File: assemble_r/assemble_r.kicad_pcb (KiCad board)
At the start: 2 copper layers, 135 x 119.3 mm, 61 parts, among them J1 Conn_01x02_Pin, SW29 SW_Push, SW30 SW_Push, SW31 SW_Push, SW32 SW_Push, SW33 SW_Push, SW34 SW_Push, SW35 SW_Push, SW36 SW_Push, SW37 SW_Push, SW38 SW_Push, SW39 SW_Push, SW40 SW_Push, SW41 SW_Push, SW42 SW_Push, SW43 SW_Push, SW44 SW_Push, SW45 SW_Push, SW46 SW_Push, SW47 SW_Push, SW48 SW_Push, SW49 SW_Push, SW50 SW_Push, SW51 SW_Push, SW52 SW_Push, SW53 SW_Push, SW54 SW_Push, SW55 SW_Push, SW56 SW_Push, U1 Micon_BLEMicroPro

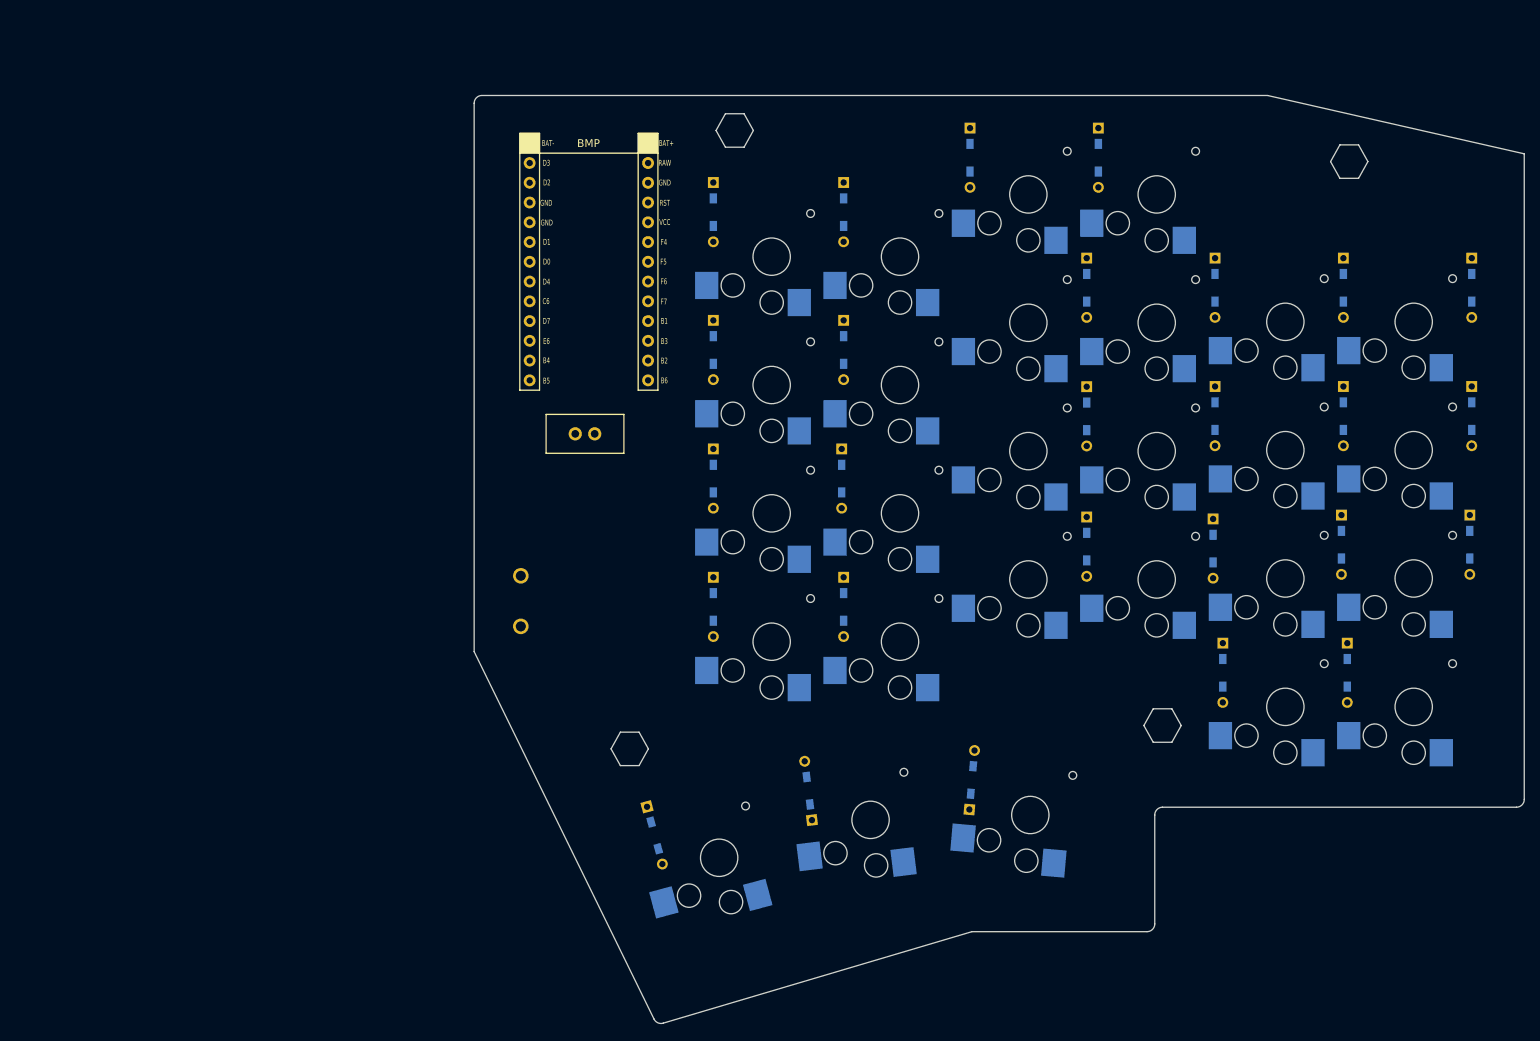
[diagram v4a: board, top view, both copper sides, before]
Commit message: feat: change key placement
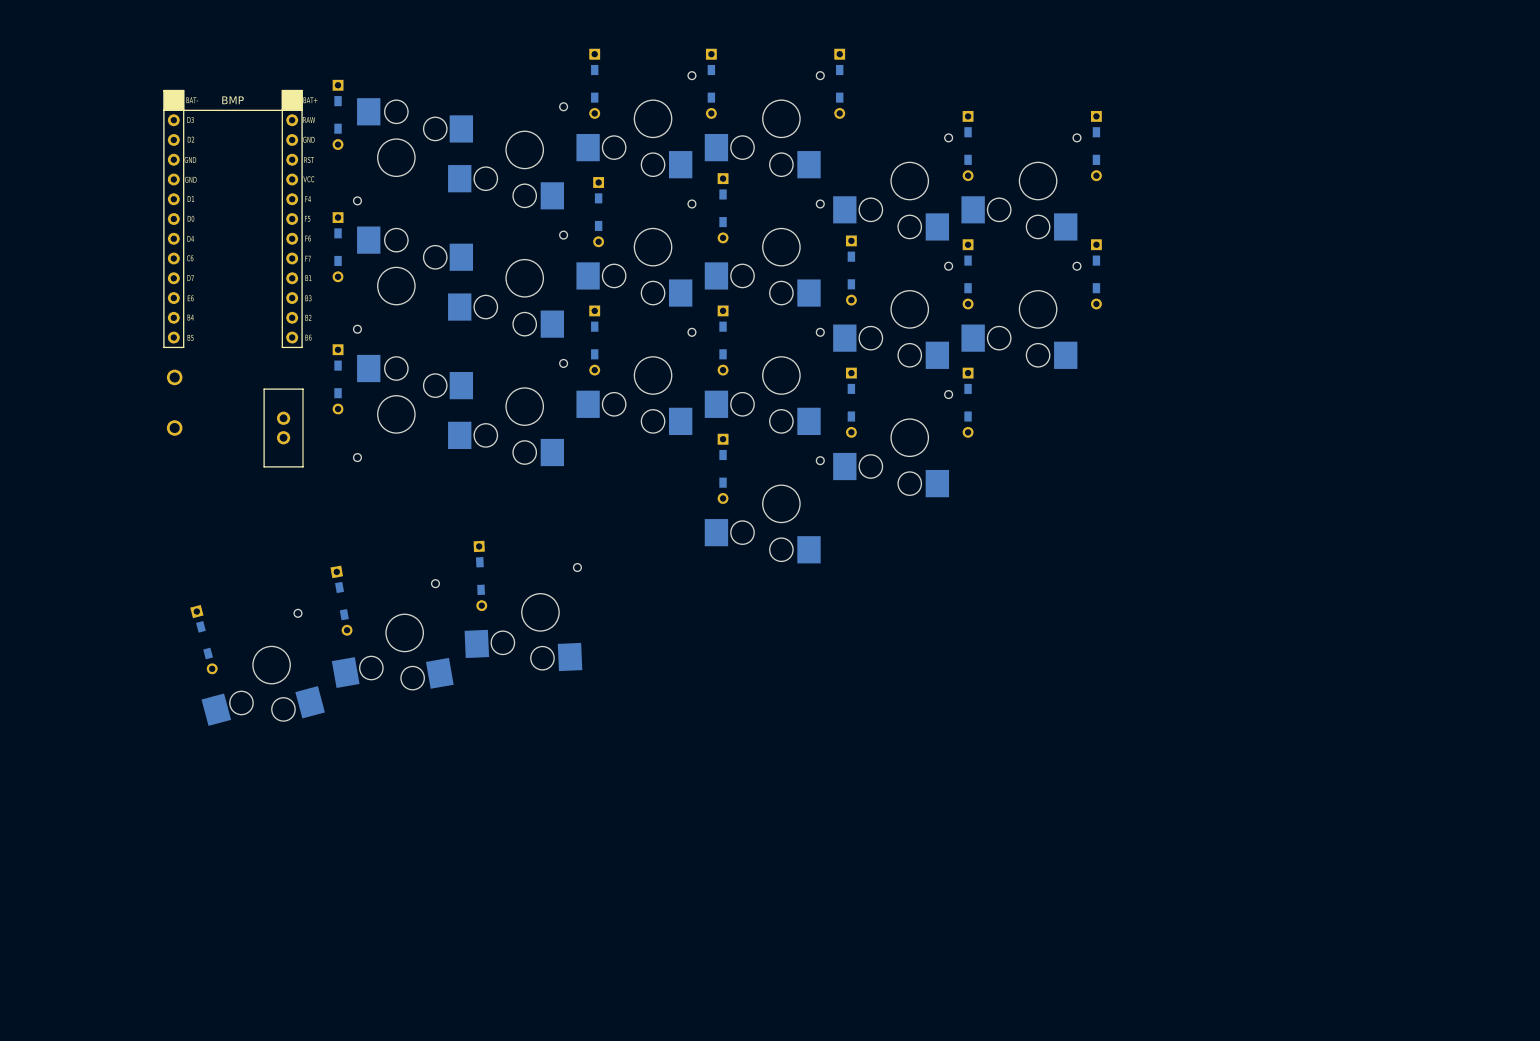
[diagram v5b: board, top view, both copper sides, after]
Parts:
- removed D44, D45, D46, D47, D48, D49, D50, D51, D52, D53, D54, D55: D, kbd_Parts:Diode_TH_SMD
- removed J1: Conn_01x02_Pin, kbd_Parts:Battery_2pin
- removed Ref** (x4): Val**, kbd_Hole:m2_Spacer_Hole_hex
- removed SW45, SW46, SW47, SW48, SW49, SW50, SW51, SW52, SW53, SW54, SW55: SW_Push, kbd_SW:Choc_v2_Hotswap_1u_16.5
- removed SW56: SW_Push, kbd_Parts:ResetSW
- removed U1: Micon_BLEMicroPro, kbd_Parts:Micon_BMP_7sKB
- added D23: D, kbd_Parts:Diode_TH_SMD, F.Cu at (63.5, 42.5)
- added D24: D, kbd_Parts:Diode_TH_SMD, F.Cu at (63.5, 59.5)
- added D25: D, kbd_Parts:Diode_TH_SMD, F.Cu at (63.5, 76.5)
- added D26: D, kbd_Parts:Diode_TH_SMD, F.Cu at (46.3, 110.0)
- added D27: D, kbd_Parts:Diode_TH_SMD, F.Cu at (96.5, 38.5)
- added D28: D, kbd_Parts:Diode_TH_SMD, F.Cu at (97.0, 55.0)
- added J23: Conn_01x02_Pin, kbd_Parts:Battery_2pin, F.Cu at (56.5, 82.8)
- added SW23: SW_Push, kbd_SW:Choc_v2_Hotswap_1u_16.5, F.Cu at (71.0, 48.0)
- added SW24: SW_Push, kbd_SW:Choc_v2_Hotswap_1u_16.5, F.Cu at (71.0, 64.5)
- added SW25: SW_Push, kbd_SW:Choc_v2_Hotswap_1u_16.5, F.Cu at (71.0, 81.0)
- added SW26: SW_Push, kbd_SW:Choc_v2_Hotswap_1u_16.5, F.Cu at (55.0, 113.2)
- added SW27: SW_Push, kbd_SW:Choc_v2_Hotswap_1u_16.5, F.Cu at (87.5, 47.0)
- added SW28: SW_Push, kbd_SW:Choc_v2_Hotswap_1u_16.5, F.Cu at (87.5, 63.5)
- added U23: Micon_BLEMicroPro, kbd_Parts:Micon_BMP_7sKB, F.Cu at (50.0, 57.7)
- SW44: footprint kbd_SW:Choc_v2_Hotswap_1u_16.5 -> kbd_Parts:ResetSW
- moved SW44 129.1 mm to (42.5, 79.5), turned to 90 degrees
- moved D43 66.9 mm to (161.0, 63.0), turned to -90 degrees
- moved D34 66.1 mm to (81.8, 101.8), turned to -87.5 degrees
- moved SW34 65.0 mm to (89.5, 106.4), turned to 2.5 degrees
- moved SW43 65.0 mm to (153.5, 67.5), turned to 0 degrees
- moved D33 64.2 mm to (113.0, 71.5), turned to -90 degrees
- moved SW33 62.6 mm to (104.0, 76.0), turned to 0 degrees
- moved D30 57.6 mm to (64.0, 105.0), turned to -80 degrees
- moved SW30 56.9 mm to (72.1, 109.1), turned to 10 degrees
- moved SW31 53.0 mm to (104.0, 43.0)
- moved SW32 53.0 mm to (104.0, 59.5)
- moved D42 51.5 mm to (161.0, 46.5)
- moved D32 51.3 mm to (113.0, 54.5)
- moved SW42 51.2 mm to (153.5, 51.0)
- moved D31 50.8 mm to (111.5, 38.5)
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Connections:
- D29 pad 1: Row0 -> Row2
- D30 pad 1: Row1 -> Row3
- D31 pad 1: Row2 -> Row0
- D32 pad 1: Row3 -> Row1
- D33 pad 1: Row4 -> Row2
- D34 pad 1: Row0 -> Row3
- D35 pad 1: Row1 -> Row0
- D36 pad 1: Row2 -> Row1
- D37 pad 1: Row3 -> Row2
- D38 pad 1: Row4 -> Row3
- D42 pad 1: Row3 -> Row0
- D43 pad 1: Row4 -> Row1
- SW29 pad 1: Col0 -> Col1
- SW30 pad 1: Col0 -> Col1
- SW31 pad 1: Col0 -> Col2
- SW32 pad 1: Col0 -> Col2
- SW33 pad 1: Col0 -> Col2
- SW34 pad 1: Col1 -> Col2
- SW35 pad 1: Col1 -> Col3
- SW36 pad 1: Col1 -> Col3
- SW37 pad 1: Col1 -> Col3
- SW38 pad 1: Col1 -> Col3
- SW39 pad 1: Col2 -> Col4
- SW40 pad 1: Col2 -> Col4
- SW41 pad 1: Col2 -> Col4
- SW42 pad 1: Col2 -> Col5
- SW43 pad 1: Col2 -> Col5
- SW44 pad 1: Col3 -> Reset
- SW44 pad 2: Net-(D44-A) -> GND
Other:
- board outline removed

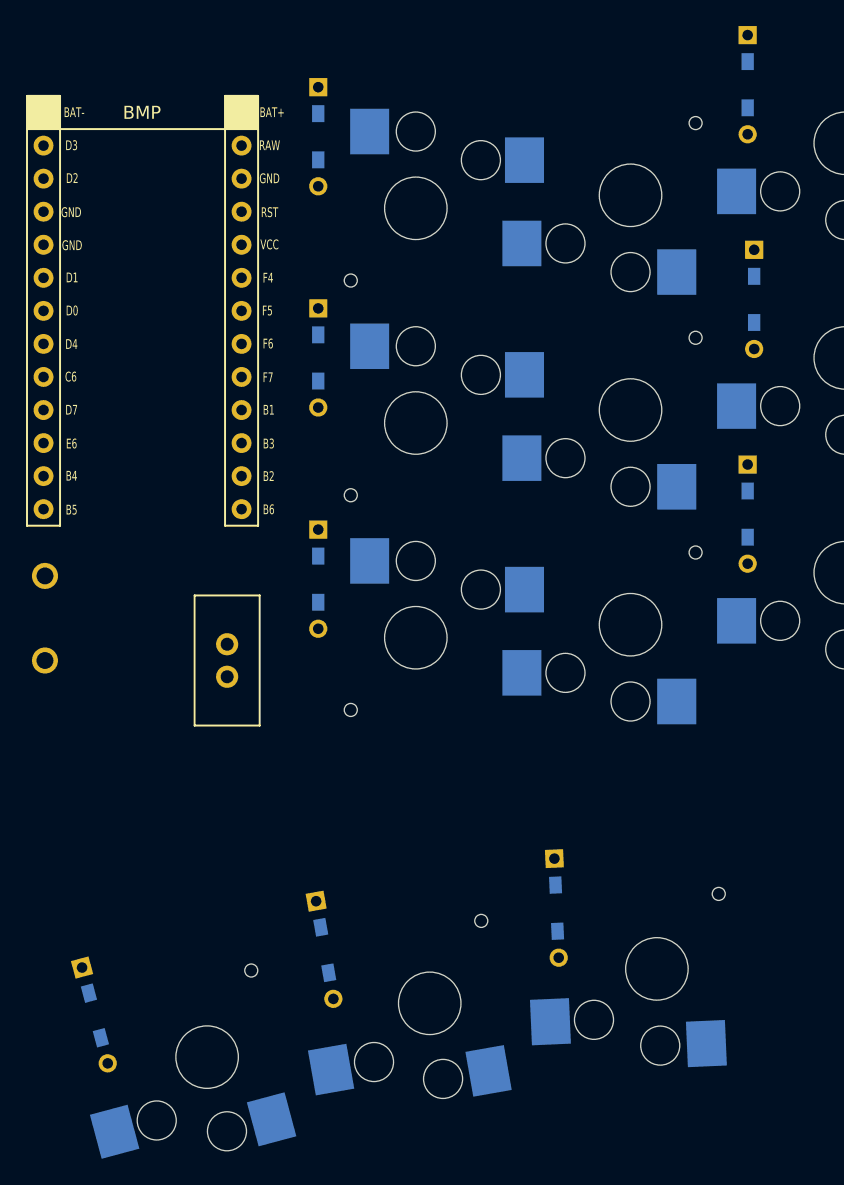
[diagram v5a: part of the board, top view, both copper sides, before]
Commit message: fix: key layout
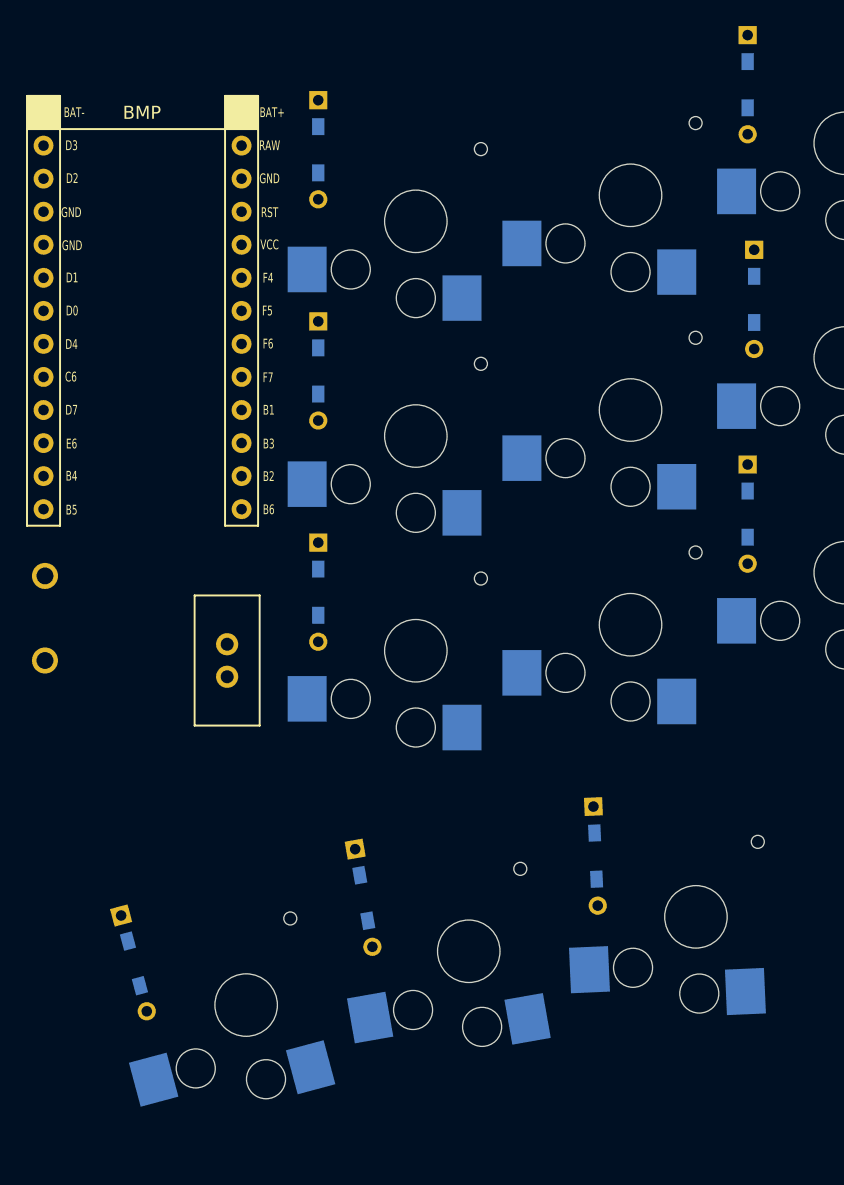
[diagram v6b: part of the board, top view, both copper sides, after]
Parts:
- moved D26 5.00 mm to (49.3, 106.0)
- moved D30 5.00 mm to (67.0, 101.0)
- moved D34 5.00 mm to (84.8, 97.8)
- moved SW26 5.00 mm to (58.0, 109.2)
- moved SW30 5.00 mm to (75.1, 105.1)
- moved SW34 5.00 mm to (92.5, 102.4)
- moved D23 1.00 mm to (63.5, 43.5)
- moved D24 1.00 mm to (63.5, 60.5)
- moved D25 1.00 mm to (63.5, 77.5)
- moved SW23 1.00 mm to (71.0, 49.0), turned to 0 degrees
- moved SW24 1.00 mm to (71.0, 65.5), turned to 0 degrees
- moved SW25 1.00 mm to (71.0, 82.0), turned to 0 degrees

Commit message: feat: add outline
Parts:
- moved D26 2.00 mm to (49.3, 104.0)
- moved D30 2.00 mm to (67.0, 99.0)
- moved D34 2.00 mm to (84.8, 95.8)
- moved SW26 2.00 mm to (58.0, 107.2)
- moved SW30 2.00 mm to (75.1, 103.1)
- moved SW34 2.00 mm to (92.5, 100.4)
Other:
- board outline added: 128.5 x 92.1 mm
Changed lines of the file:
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@@
 	(footprint "kbd_SW:Choc_v2_Hotswap_1u_16.5"
 		(layer "F.Cu")
-		(at 57.95969 109.229467 15)
+		(at 57.95969 107.229467 15)
 		(property "Reference" "SW26"
 			(at -5.08 -6.35 15)
@@
 	(footprint "kbd_Parts:Diode_TH_SMD"
 		(layer "F.Cu")
-		(at 84.814316 97.781712 -87.5)
+		(at 84.814316 95.781712 -87.5)
 		(descr "Resitance 3 pas")
 		(tags "R")
@@
 	(footprint "kbd_Parts:Diode_TH_SMD"
 		(layer "F.Cu")
-		(at 49.337035 106.027055 -75)
+		(at 49.337035 104.027055 -75)
 		(descr "Resitance 3 pas")
 		(tags "R")
@@
 	(footprint "kbd_SW:Choc_v2_Hotswap_1u_16.5"
 		(layer "F.Cu")
-		(at 75.06811 105.095004 10)
+		(at 75.06811 103.095004 10)
 		(property "Reference" "SW30"
 			(at -5.08 -6.349999 10)
@@
 		)
 		(fp_line
-			(start -0.850002 8.2)
+			(start -0.850003 8.2)
 			(end -0.85 3.6)
 			(stroke
@@
 	(footprint "kbd_Parts:Diode_TH_SMD"
 		(layer "F.Cu")
-		(at 67 101 -80)
+		(at 67 99 -80)
 		(descr "Resitance 3 pas")
 		(tags "R")
@@
 		)
 		(pad "1" thru_hole rect
-			(at -3.810002 0 280)
+			(at -3.810003 0 280)
 			(size 1.397 1.397)
 			(drill 0.8128)
@@
 		)
 		(pad "2" thru_hole circle
-			(at 3.810002 0 280)
+			(at 3.810003 0 280)
 			(size 1.397 1.397)
 			(drill 0.8128)
@@
 	(footprint "kbd_SW:Choc_v2_Hotswap_1u_16.5"
 		(layer "F.Cu")
-		(at 92.525274 102.449808 2.5)
+		(at 92.525274 100.449808 2.5)
 		(property "Reference" "SW34"
 			(at -5.08 -6.35 2.5)
@@
 		)
 		(fp_line
-			(start -4.6 6.000002)
+			(start -4.6 6.000003)
 			(end -4.6 1.4)
 			(stroke
@@
 		)
 		(fp_line
-			(start -1.3 7.989998)
+			(start -1.3 7.989997)
 			(end -1.3 3.6)
 			(stroke
@@
 		(fp_line
 			(start -0.4 8.2)
-			(end -0.399998 3.6)
+			(end -0.399997 3.6)
 			(stroke
 				(width 0.15)
@@
 		)
 		(pad "" np_thru_hole circle
-			(at 5.000002 -5.55 2.5)
+			(at 5.000003 -5.55 2.5)
 			(size 1 1)
 			(drill oval 1)
@@
 		(embedded_fonts no)
 	)
+	(gr_arc
+		(start 48.161805 121.849991)
+		(mid 47.434731 121.73721)
+		(end 46.981573 121.15755)
+		(stroke
+			(width 0.05)
+			(type default)
+		)
+		(layer "Edge.Cuts")
+	)
+	(gr_line
+		(start 107 105.5)
+		(end 130.731933 105.5)
+		(stroke
+			(width 0.05)
+			(type default)
+		)
+		(layer "Edge.Cuts")
+	)
+	(gr_line
+		(start 85 113.5)
+		(end 105 113.5)
+		(stroke
+			(width 0.05)
+			(type default)
+		)
+		(layer "Edge.Cuts")
+	)
+	(gr_line
+		(start 94 29.75)
+		(end 130 29.75)
+		(stroke
+			(width 0.05)
+			(type default)
+		)
+		(layer "Edge.Cuts")
+	)
+	(gr_line
+		(start 131.232123 105.365916)
+		(end 165.992057 85.287098)
+		(stroke
+			(width 0.05)
+			(type default)
+		)
+		(layer "Edge.Cuts")
+	)
+	(gr_arc
+		(start 131.232123 105.365916)
+		(mid 130.990856 105.465889)
+		(end 130.731933 105.5)
+		(stroke
+			(width 0.05)
+			(type default)
+		)
+		(layer "Edge.Cuts")
+	)
+	(gr_arc
+		(start 106 112.5)
+		(mid 105.707107 113.207107)
+		(end 105 113.5)
+		(stroke
+			(width 0.05)
+			(type default)
+		)
+		(layer "Edge.Cuts")
+	)
+	(gr_line
+		(start 37 32)
+		(end 37 32)
+		(stroke
+			(width 0.05)
+			(type default)
+		)
+		(layer "Edge.Cuts")
+	)
+	(gr_line
+		(start 48.161805 121.849991)
+		(end 85 113.5)
+		(stroke
+			(width 0.05)
+			(type default)
+		)
+		(layer "Edge.Cuts")
+	)
+	(gr_line
+		(start 130 29.75)
+		(end 165.733121 38.316159)
+		(stroke
+			(width 0.05)
+			(type default)
+		)
+		(layer "Edge.Cuts")
+	)
+	(gr_line
+		(start 38 93)
+		(end 46.981573 121.15755)
+		(stroke
+			(width 0.05)
+			(type default)
+		)
+		(layer "Edge.Cuts")
+	)
+	(gr_line
+		(start 128.5 29.5)
+		(end 128.5 29.5)
+		(stroke
+			(width 0.05)
+			(type default)
+		)
+		(layer "Edge.Cuts")
+	)
+	(gr_line
+		(start 94 29.75)
+		(end 81 32)
+		(stroke
+			(width 0.05)
+			(type default)
+		)
+		(layer "Edge.Cuts")
+	)
+	(gr_arc
+		(start 38 33)
+		(mid 38.292893 32.292889)
+		(end 39 32)
+		(stroke
+			(width 0.05)
+			(type default)
+		)
+		(layer "Edge.Cuts")
+	)
+	(gr_arc
+		(start 166.5 84.416535)
+		(mid 166.363729 84.920491)
+		(end 165.992057 85.287098)
+		(stroke
+			(width 0.05)
+			(type default)
+		)
+		(layer "Edge.Cuts")
+	)
+	(gr_line
+		(start 81 32)
+		(end 39 32)
+		(stroke
+			(width 0.05)
+			(type default)
+		)
+		(layer "Edge.Cuts")
+	)
+	(gr_line
+		(start 166.5 39.288607)
+		(end 166.5 84.416535)
+		(stroke
+			(width 0.05)
+			(type default)
+		)
+		(layer "Edge.Cuts")
+	)
+	(gr_arc
+		(start 106 106.5)
+		(mid 106.292893 105.792893)
+		(end 107 105.5)
+		(stroke
+			(width 0.05)
+			(type default)
+		)
+		(layer "Edge.Cuts")
+	)
+	(gr_line
+		(start 38 33)
+		(end 38 93)
+		(stroke
+			(width 0.05)
+			(type default)
+		)
+		(layer "Edge.Cuts")
+	)
+	(gr_arc
+		(start 165.733121 38.316159)
+		(mid 166.285217 38.669379)
+		(end 166.5 39.288607)
+		(stroke
+			(width 0.05)
+			(type default)
+		)
+		(layer "Edge.Cuts")
+	)
+	(gr_line
+		(start 106 112.5)
+		(end 106 106.5)
+		(stroke
+			(width 0.05)
+			(type default)
+		)
+		(layer "Edge.Cuts")
+	)
 	(embedded_fonts no)
